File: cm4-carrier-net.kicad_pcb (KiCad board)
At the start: 4 copper layers, 90 x 40 mm, 59 parts, among them J1 USB_C_Receptacle_USB2.0, J2 Micro_SD_Card, J3 Abracon_ARJM11-502, J5 block, Q1 DMP2066LSN, SW1 BOOT, SW2 GLOBAL_EN, SW3 USB_OTG, U1 TPS54302, U5 Compute_Module_4_Functional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

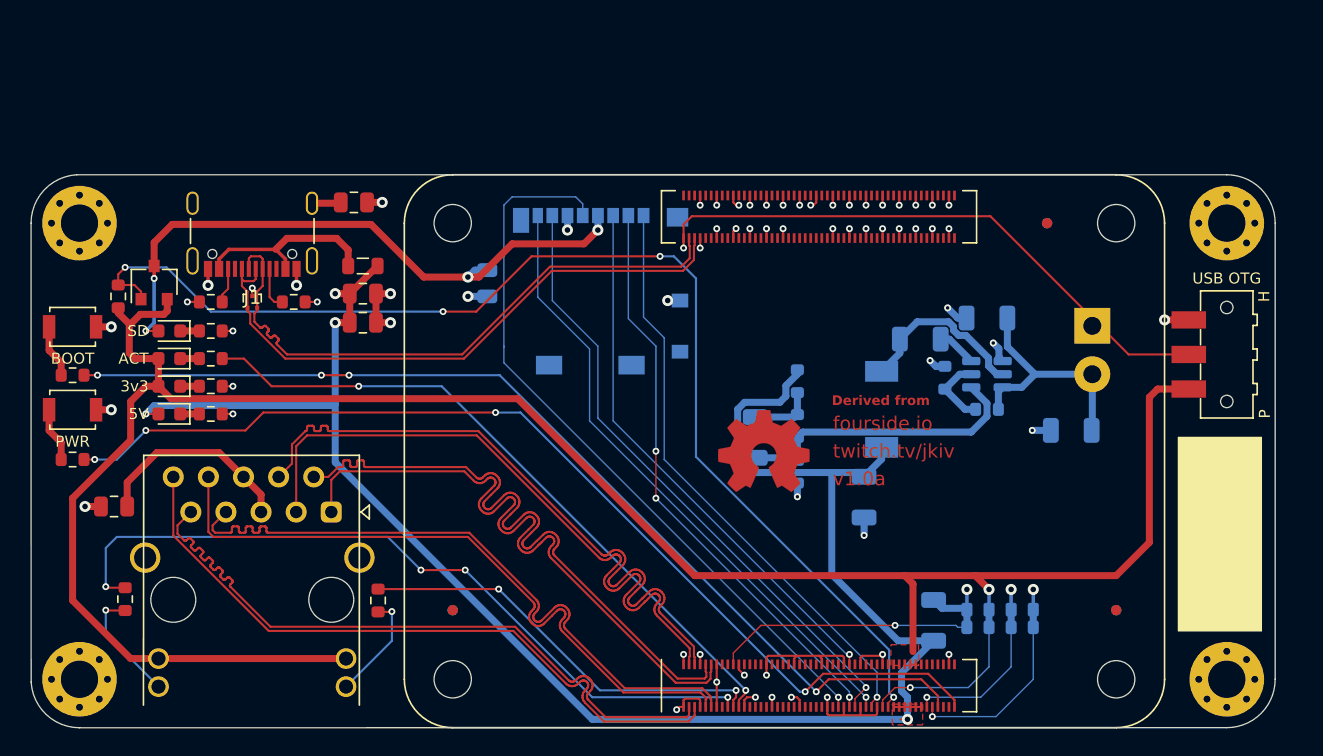
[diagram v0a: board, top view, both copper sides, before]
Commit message: added power protection and some layout changes
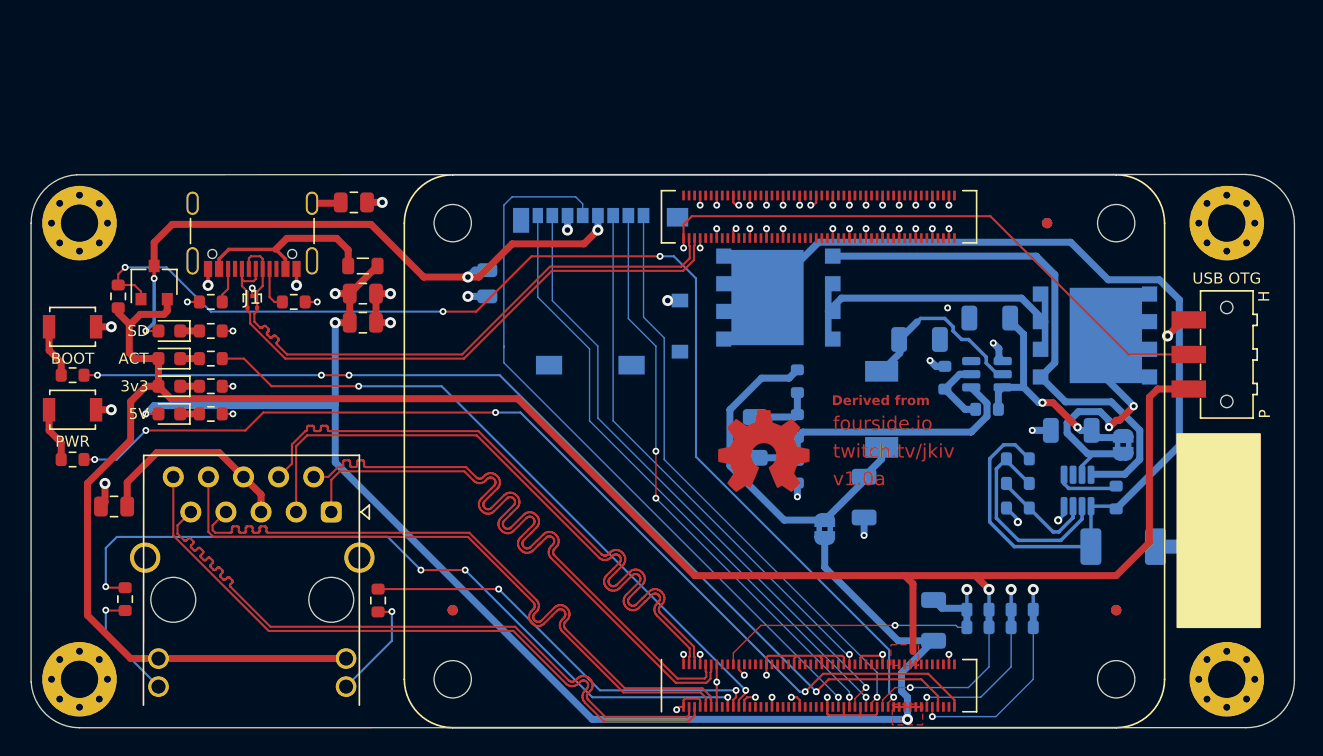
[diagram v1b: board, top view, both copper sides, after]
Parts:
- added D5: D, Diode_SMD:D_2010_5025Metric_Pad1.52x2.65mm_HandSolder, B.Cu at (159.0, 120.9)
- added JP5: SolderJumper_2_Bridged, Jumper:SolderJumper-2_P1.3mm_Bridged2Bar_RoundedPad1.0x1.5mm, B.Cu at (159.0, 113.5)
- added JP6: SolderJumper_2_Bridged, Jumper:SolderJumper-2_P1.3mm_Bridged2Bar_RoundedPad1.0x1.5mm, B.Cu at (137.4, 119.6)
- added Q2: FDMT800152DC, Package_TO_SOT_SMD:PQFN_8x8, B.Cu at (134.1, 102.9)
- added Q3: FDMT800152DC, Package_TO_SOT_SMD:PQFN_8x8, B.Cu at (157.0, 105.6)
- added R17: 510kOhm, Resistor_SMD:R_0603_1608Metric, B.Cu at (158.5, 117.3)
- added R18: 2740kOhm, Resistor_SMD:R_0603_1608Metric, B.Cu at (151.4, 114.6)
- added R19: 215kOhm, Resistor_SMD:R_0603_1608Metric, B.Cu at (151.4, 116.3)
- added R20: 84.5kOhm, Resistor_SMD:R_0603_1608Metric, B.Cu at (151.4, 118.1)
- added U2: LTC4365TS8, Package_TO_SOT_SMD:TSOT-23-8, B.Cu at (155.7, 116.8)
- moved J5 19.7 mm to (167.6, 121.4), turned to 90 degrees
- moved C7 0.20 mm to (149.4, 104.4)
- moved C8 0.06 mm to (144.3, 105.9)
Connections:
- C10 pad 1: +5V -> Net-(JP6-B)
- C6 pad 1: Net-(J5-Pin_2) -> +12V
- C7 pad 1: Net-(J5-Pin_2) -> +12V
- C9 pad 1: +5V -> Net-(JP6-B)
- J5 pad 2: Net-(J5-Pin_2) -> Net-(D5-A)
- L1 pad 2: +5V -> Net-(JP6-B)
- R14 pad 1: +5V -> Net-(JP6-B)
- R5 pad 1: Net-(J5-Pin_2) -> +12V
- U1 pad 3: Net-(J5-Pin_2) -> +12V
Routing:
- net Net-(D5-K): track 0.00 -> 71.5 mm
- net Net-(Q2-G): track 0.00 -> 39.3 mm
- net +5V: track 129.5 -> 102.7 mm
- net Net-(JP6-B): track 0.00 -> 26.0 mm
- net Net-(JP5-A): track 0.00 -> 21.9 mm, vias 0 -> 2
- net +12V: track 0.00 -> 17.9 mm, vias 0 -> 2
- net Net-(J5-Pin_2): track 17.6 -> 0.00 mm
- net Net-(Q2-S): track 0.00 -> 16.8 mm
- net Net-(U2-UV): track 0.00 -> 15.5 mm
- net Net-(U2-OV): track 0.00 -> 7.60 mm
- net Net-(D5-A): track 0.00 -> 7.51 mm
- net Net-(U2-~{SHDN}): track 0.00 -> 4.63 mm
- net Net-(U1-BOOT): track 2.87 -> 0.00 mm
- net GND: track 88.3 -> 90.1 mm, vias 69 -> 71
- net +3V3: track 153.1 -> 152.2 mm
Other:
- board size 90 x 40 mm -> 91.4 x 40 mm

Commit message: a couple of changes
fully removed cm4!
added orange pi cm4 footprint.
added extra usb 2 port.
removed unneeded diode.
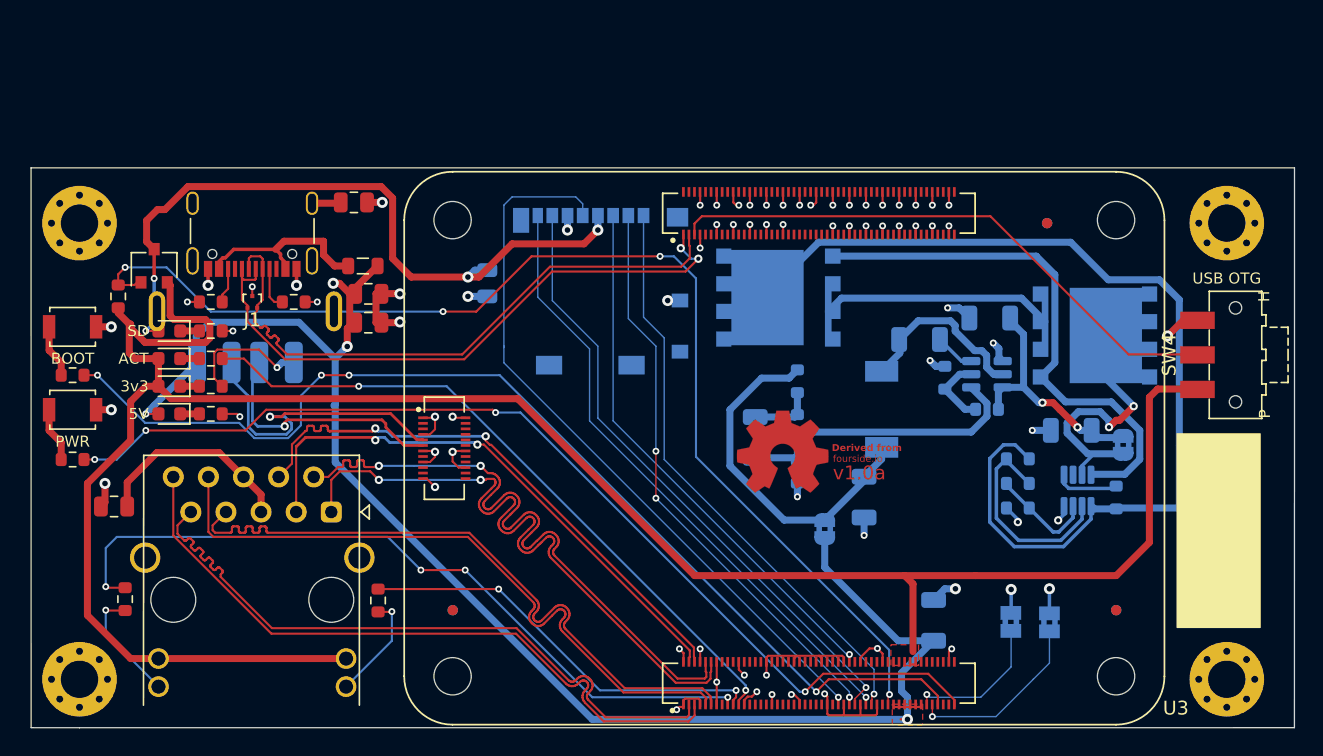
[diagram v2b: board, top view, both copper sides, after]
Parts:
- removed D5: D, Diode_SMD:D_2010_5025Metric_Pad1.52x2.65mm_HandSolder
- removed JP1: eMMC, jkiv-library:J_Small_NC
- removed JP2: ~WL_nDisable, jkiv-library:J_Small_NC
- removed JP3: ~BT_nDisable, jkiv-library:J_Small_NC
- removed JP4: EEPROM_nWP, jkiv-library:J_Small_NC
- removed SW3: USB_OTG, Button_Switch_SMD:SW_SPDT_CK-JS102011SAQN
- removed U5: Compute_Module_4_Functional, RPi_Compute_Module_4:Raspberry-Pi-4-Compute-Module
- added J6: USB_A, Connector_USB:USB_A_Receptacle_GCT_USB1046, B.Cu at (95.5, 100.3)
- added JP7: ~WL_nDisable, Jumper:SolderJumper-2_P1.3mm_Bridged2Bar_Pad1.0x1.5mm, B.Cu at (150.9, 126.3)
- added JP8: ~BT_nDisable, Jumper:SolderJumper-2_P1.3mm_Bridged2Bar_Pad1.0x1.5mm, B.Cu at (153.7, 126.4)
- added SW4: USB_OTG, Button_Switch_SMD:SW_SPDT_CK-JS102011SAQN, F.Cu at (167.1, 107.0)
- added U3: ORANGE_PI_CM4, Orange-Pi-CM4:MODULE_ORANGE_PI_CM4, F.Cu at (134.5, 113.8)
- moved LOGO1 1.37 mm to (134.4, 114.0)
- moved Q1 1.22 mm to (88.9, 100.6)
- moved C2 0.39 mm to (104.4, 102.6)
- moved C1 0.39 mm to (104.4, 104.7)
- moved J5 0.25 mm to (167.6, 121.6)
- turned C10 to -90 degrees
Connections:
- C10 pad 1: Net-(JP6-B) -> GND
- C10 pad 2: GND -> +5V
- D2 pad 2: +3V3 -> +3.3V
- D3 pad 2: +3V3 -> +3.3V
- J3 pad 13: +3V3 -> +3.3V
- J5 pad 2: Net-(D5-A) -> Net-(J5-Pin_2)
- Q1 pad 2: +3V3 -> +3.3V
- Q2 pad 3: Net-(D5-K) -> Net-(J5-Pin_2)
- R17 pad 1: Net-(D5-K) -> Net-(J5-Pin_2)
- R18 pad 1: Net-(D5-K) -> Net-(J5-Pin_2)
- R8 pad 2: +3V3 -> +3.3V
- U2 pad 1: Net-(D5-K) -> Net-(J5-Pin_2)
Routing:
- net +3.3V: track 0.00 -> 158.7 mm
- net +3V3: track 152.2 -> 0.00 mm, vias 1 -> 0
- net Net-(J5-Pin_2): track 0.00 -> 77.5 mm
- net Net-(D5-K): track 71.5 -> 0.00 mm
- net GND: track 90.1 -> 115.7 mm, vias 71 -> 76
- net /USB-: track 0.00 -> 22.8 mm, vias 0 -> 1
- net Net-(U5J-EEPROM_nWP): track 18.6 -> 0.00 mm, vias 1 -> 0
- net /USB+: track 0.00 -> 18.2 mm, vias 0 -> 1
- net Net-(U3A-~{BT_DIS}): track 0.00 -> 13.4 mm, vias 0 -> 1
- net Net-(U5J-~{BT_nDisable}): track 12.9 -> 0.00 mm, vias 1 -> 0
- net Net-(U5I-SD_VDD_Override): track 12.1 -> 0.00 mm, vias 1 -> 0
- net Net-(U3A-~{WL_DIS}): track 0.00 -> 10.9 mm, vias 0 -> 1
- net Net-(U5J-~{WL_nDisable}): track 10.6 -> 0.00 mm, vias 1 -> 0
- net /E0_TR1+: track 50.0 -> 41.1 mm, vias 0 -> 2
- net /E0_TR1-: track 50.0 -> 41.4 mm, vias 0 -> 2
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- added copper zone on F.Cu, net +3.3V
- removed copper zone on F.Cu, net +3V3
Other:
- board size 91.4 x 40 mm -> 91.4 x 40.5 mm
- board text added: "These should probably be toggles, but I don't feel like making more space for unnecessary things."
- board text removed: "eMMC"
- board text removed: "twitch.tv/jkiv"
- board text removed: "~{EEPROM}"

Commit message: changed some things
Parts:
- moved R12 1.49 mm to (94.5, 105.3)
- moved D4 1.44 mm to (91.4, 105.3)
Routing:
- net +3.3V: track 158.7 -> 161.5 mm
- net /SD_PWR: track 52.4 -> 54.2 mm

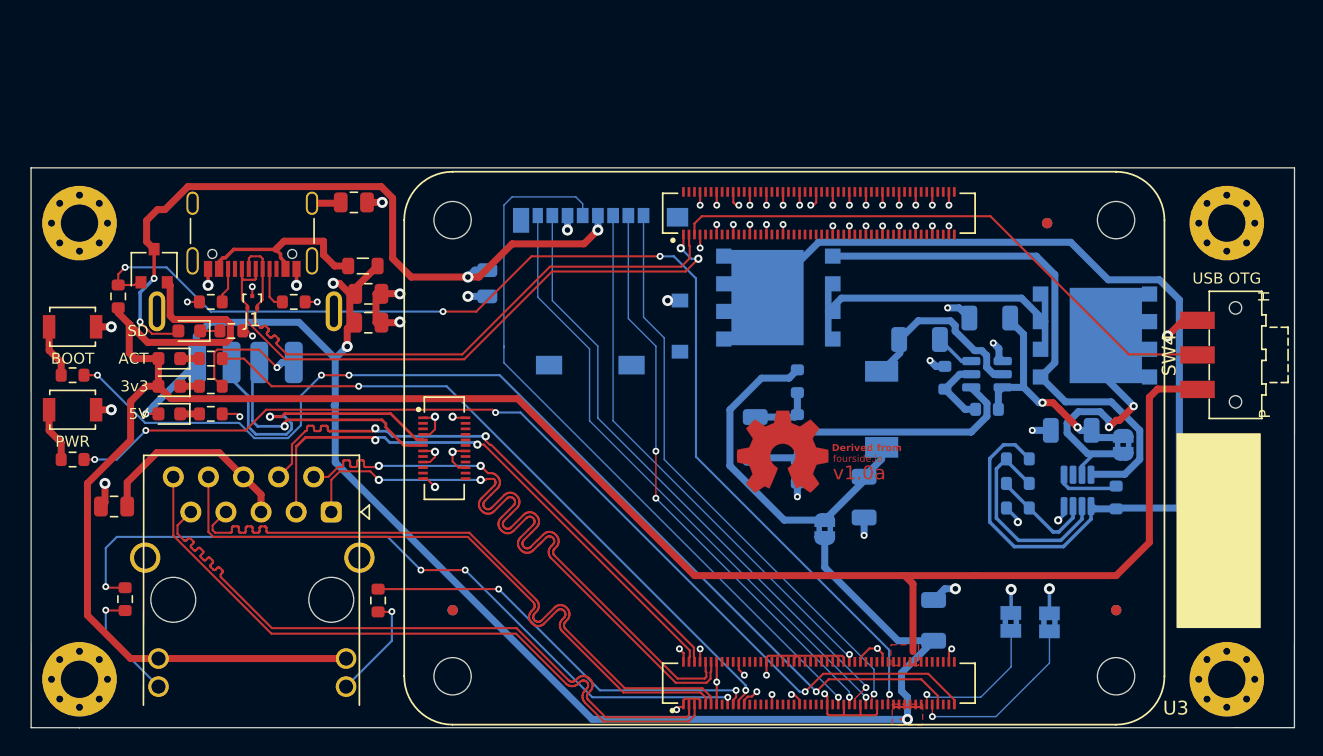
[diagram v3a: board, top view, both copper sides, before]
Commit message: added a pin header for the daughter board
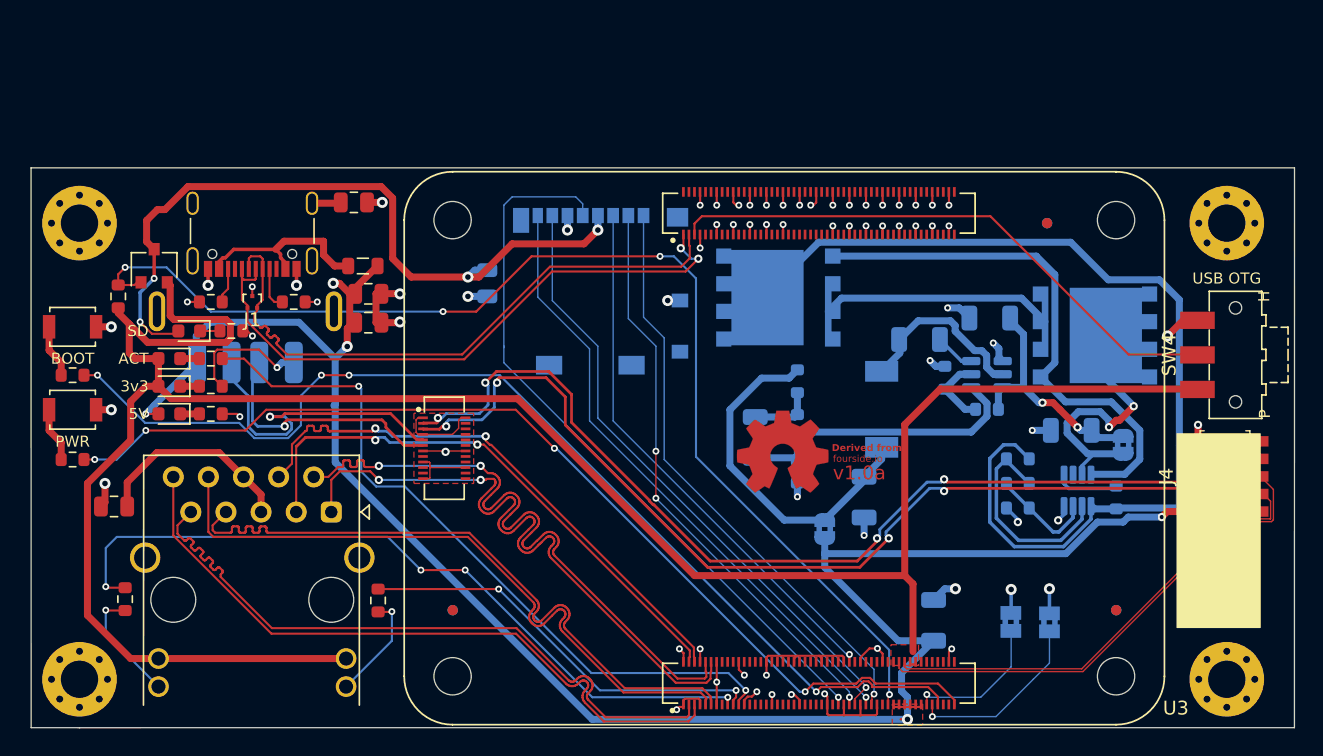
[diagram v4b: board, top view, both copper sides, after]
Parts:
- added J4: 20021121-00010C4LF, digikey-footprints:PinHeader_2x5_P1.27mm, F.Cu at (166.4, 115.8)
- moved J5 3.34 mm to (167.3, 124.9)
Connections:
- U3 pad JP1_80: unconnected-(U3A-I2C1_SCL_M0-PadJP1_80) -> /I2C1_SCL-
- U3 pad JP1_82: unconnected-(U3A-I2C1_SDA_M0-PadJP1_82) -> /I2C1_SDA+
- U3 pad JP3_3: unconnected-(U3C-USB2_HOST3_DM-PadJP3_3) -> /USB1-
- U3 pad JP3_5: unconnected-(U3C-USB2_HOST3_DP-PadJP3_5) -> /USB1+
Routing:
- net /USB1-: track 0.00 -> 69.0 mm, vias 0 -> 4
- net /USB1+: track 0.00 -> 69.0 mm, vias 0 -> 4
- net /I2C1_SCL-: track 0.00 -> 36.3 mm
- net /I2C1_SDA+: track 0.00 -> 34.2 mm
- net +5V: track 107.4 -> 139.6 mm, vias 4 -> 5
- net GND: track 115.8 -> 124.8 mm, vias 76 -> 73
- net /PI_LED_nACT: track 49.4 -> 52.7 mm
- net Net-(J5-Pin_2): track 77.5 -> 78.6 mm
- added copper zone on F.Cu, net GND

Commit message: moved a trace
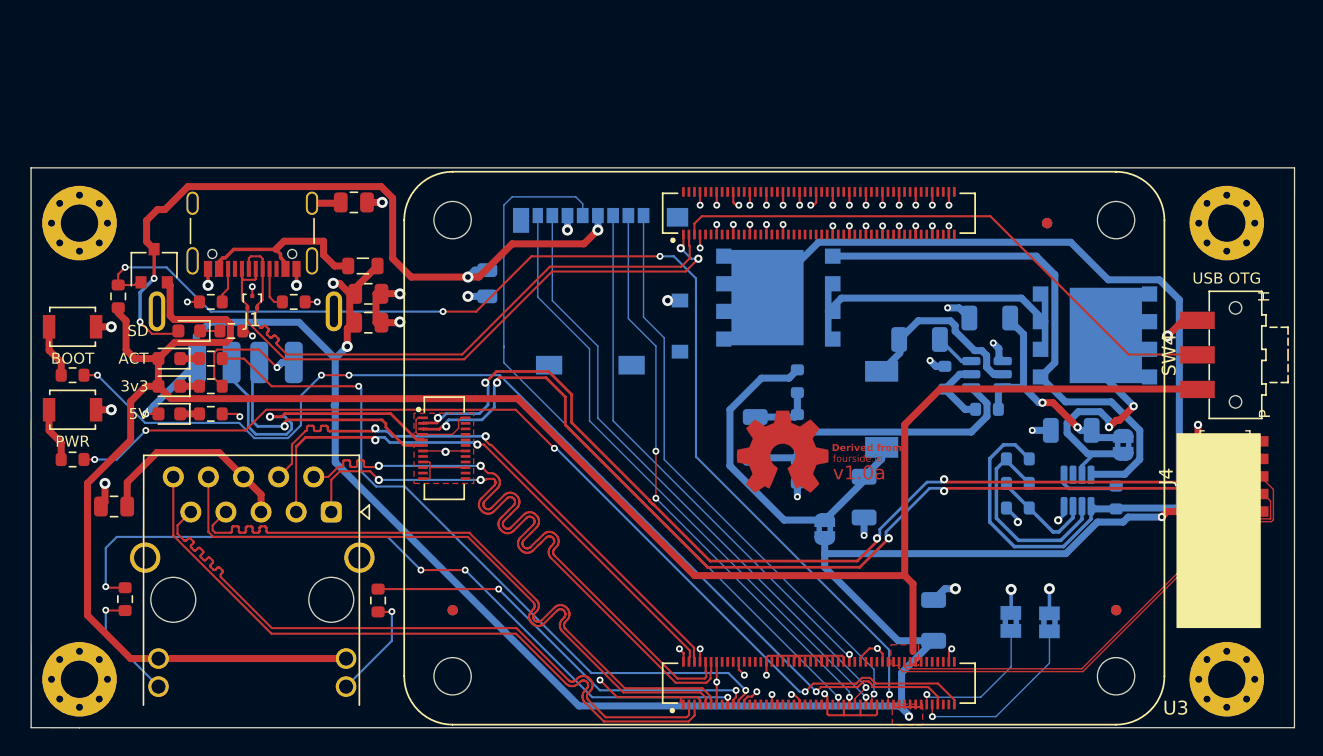
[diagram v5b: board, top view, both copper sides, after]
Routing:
- net GND: track 124.8 -> 130.9 mm
- net +3.3V: track 161.7 -> 159.5 mm
- net +5V: track 139.6 -> 138.1 mm

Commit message: added thingies
began creating daughter board and added stm32 for led control
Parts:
- added U4: STM32C011J4Mx, Package_DFN_QFN:ST_UFQFPN-20_3x3mm_P0.5mm, B.Cu at (166.3, 115.6)
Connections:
- J4 pad 3: /I2C1_SDA+ -> /LED_DRIVER_RST
- J4 pad 5: /I2C1_SCL- -> /I2C_TO_DB_SCL
- J4 pad 7: unconnected-(J4-Pad7) -> /I2C_TO_DB_SDA
- J4 pad 8: unconnected-(J4-Pad8) -> +3.3V
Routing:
- net /I2C_TO_DB_SDA: track 0.00 -> 9.37 mm, vias 0 -> 1
- net /I2C_TO_DB_SCL: track 0.00 -> 7.79 mm, vias 0 -> 1
- net /LED_DRIVER_RST: track 0.00 -> 5.47 mm, vias 0 -> 1
- net +3.3V: track 159.5 -> 164.2 mm, vias 0 -> 1
- net /I2C1_SCL-: track 36.3 -> 34.0 mm, vias 0 -> 1
- net /I2C1_SDA+: track 34.2 -> 32.8 mm, vias 0 -> 1
- net GND: track 130.9 -> 132.1 mm, vias 73 -> 74
